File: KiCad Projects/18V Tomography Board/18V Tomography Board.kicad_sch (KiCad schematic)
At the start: 39 parts, among them J1 CONREVSMA001-G, J10 CONREVSMA001-G, J11 CONREVSMA001-G, J12 CONREVSMA001-G, J13 CONREVSMA001-G, J14 CONREVSMA001-G, J15 CONREVSMA001-G, J16 CONREVSMA001-G, J2 CONREVSMA001-G, J3 CONREVSMA001-G, J4 CONREVSMA001-G, J5 CONREVSMA001-G, J6 CONREVSMA001-G, J7 CONREVSMA001-G, J8 CONREVSMA001-G, J9 CONREVSMA001-G, U1 HV2707T-C/R8X, U2 HV2707T-C/R8X, U3 OPA365xxDBV, U4 OPA365xxDBV

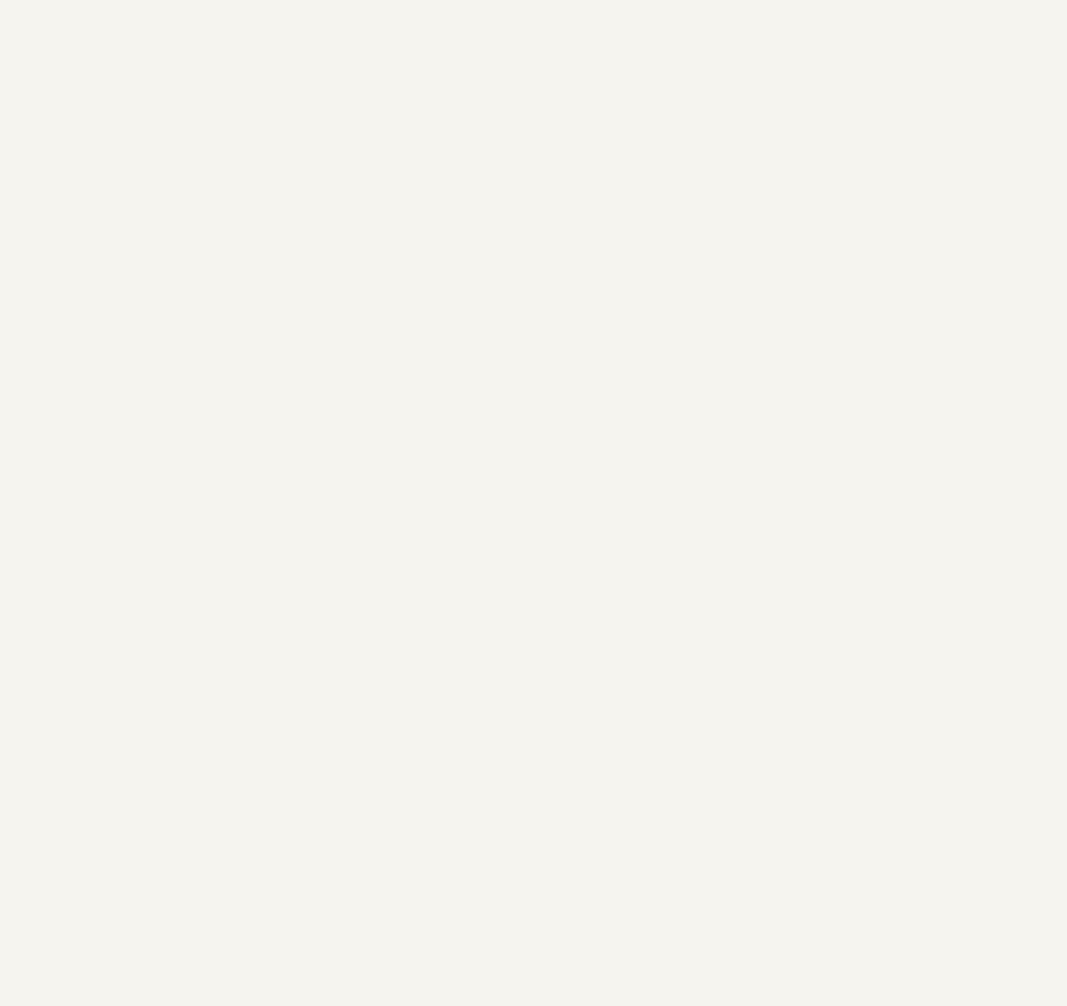
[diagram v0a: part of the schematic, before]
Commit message: added a new project and a new components for the updated pico breakout board
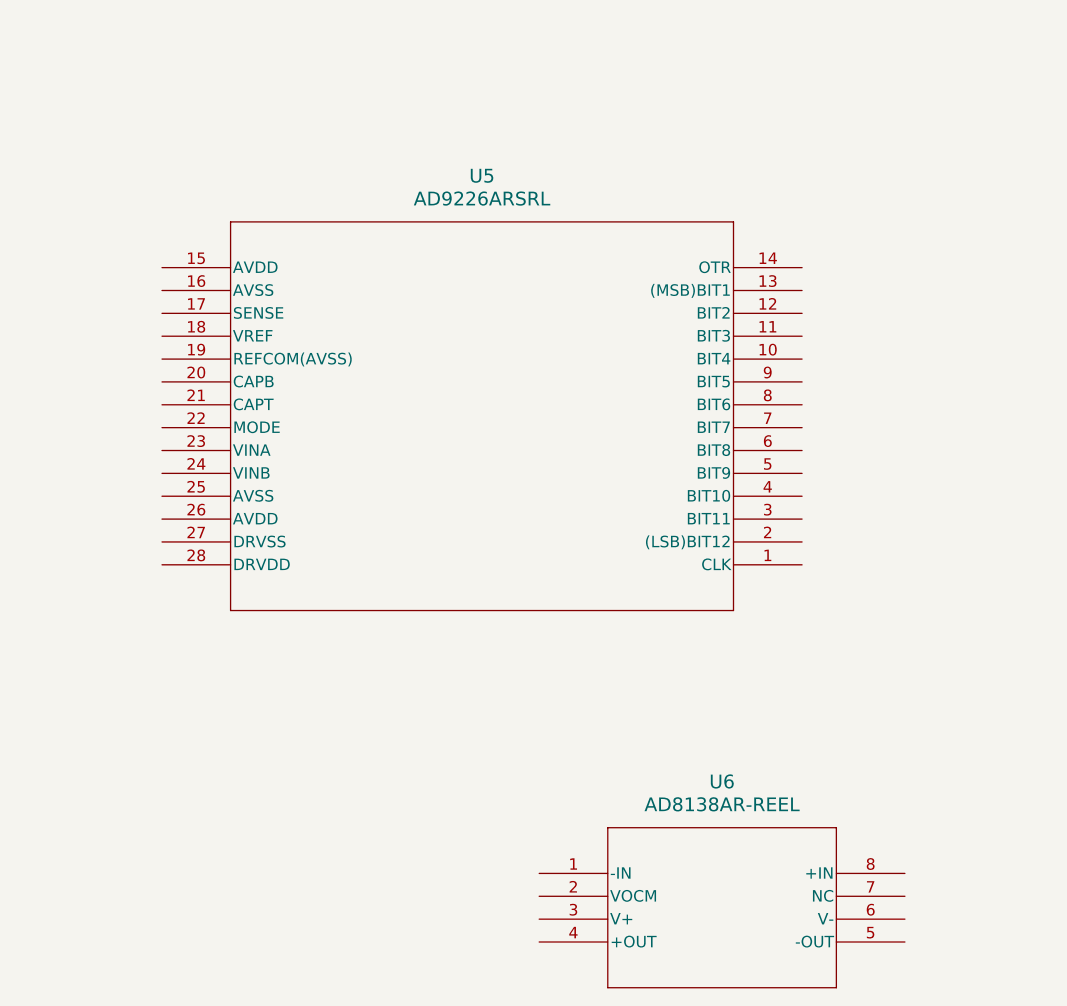
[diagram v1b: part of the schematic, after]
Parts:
- added U5: AD9226ARSRL, RS_28_ADI, symbol AD9226:AD9226ARSRL
- added U6: AD8138AR-REEL, R_8_ADI, symbol AD8138:AD8138AR-REEL
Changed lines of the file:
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@@
+	)
+	(symbol
+		(lib_id "AD8138:AD8138AR-REEL")
+		(at 537.21 679.45 0)
+		(unit 1)
+		(body_style 1)
+		(exclude_from_sim no)
+		(in_bom yes)
+		(on_board yes)
+		(in_pos_files yes)
+		(dnp no)
+		(fields_autoplaced yes)
+		(property "Reference" "U6"
+			(at 557.53 669.29 0)
+			(show_name no)
+			(do_not_autoplace no)
+			(effects
+				(font
+					(size 1.524 1.524)
+				)
+			)
+		)
+		(property "Value" "AD8138AR-REEL"
+			(at 557.53 671.83 0)
+			(show_name no)
+			(do_not_autoplace no)
+			(effects
+				(font
+					(size 1.524 1.524)
+				)
+			)
+		)
+		(property "Footprint" "R_8_ADI"
+			(at 537.21 679.45 0)
+			(hide yes)
+			(show_name no)
+			(do_not_autoplace no)
+			(effects
+				(font
+					(size 1.27 1.27)
+					(italic yes)
+				)
+			)
+		)
+		(property "Datasheet" "AD8138AR-REEL"
+			(at 537.21 679.45 0)
+			(hide yes)
+			(show_name no)
+			(do_not_autoplace no)
+			(effects
+				(font
+					(size 1.27 1.27)
+					(italic yes)
+				)
+			)
+		)
+		(property "Description" ""
+			(at 537.21 679.45 0)
+			(hide yes)
+			(show_name no)
+			(do_not_autoplace no)
+			(effects
+				(font
+					(size 1.27 1.27)
+				)
+			)
+		)
+		(pin "6"
+		)
+		(pin "2"
+		)
+		(pin "5"
+		)
+		(pin "7"
+		)
+		(pin "3"
+		)
+		(pin "1"
+		)
+		(pin "8"
+		)
+		(pin "4"
+		)
+		(instances
+			(project "18V Tomography Board"
+				(path "/8ecf61f3-91a2-40b2-9601-c3a56e620970"
+					(reference "U6")
+					(unit 1)
+				)
+			)
+		)
 	)
 	(symbol
@@
 					(unit 1)
 				)
+			)
+		)
+	)
+	(symbol
+		(lib_id "AD9226:AD9226ARSRL")
+		(at 566.42 645.16 180)
+		(unit 1)
+		(body_style 1)
+		(exclude_from_sim no)
+		(in_bom yes)
+		(on_board yes)
+		(in_pos_files yes)
+		(dnp no)
+		(fields_autoplaced yes)
+		(property "Reference" "U5"
+			(at 530.86 601.98 0)
+			(show_name no)
+			(do_not_autoplace no)
+			(effects
+				(font
+					(size 1.524 1.524)
+				)
+			)
+		)
+		(property "Value" "AD9226ARSRL"
+			(at 530.86 604.52 0)
+			(show_name no)
+			(do_not_autoplace no)
+			(effects
+				(font
+					(size 1.524 1.524)
+				)
+			)
+		)
+		(property "Footprint" "RS_28_ADI"
+			(at 566.42 645.16 0)
+			(hide yes)
+			(show_name no)
+			(do_not_autoplace no)
+			(effects
+				(font
+					(size 1.27 1.27)
+					(italic yes)
+				)
+			)
+		)
+		(property "Datasheet" "AD9226ARSRL"
+			(at 566.42 645.16 0)
+			(hide yes)
+			(show_name no)
+			(do_not_autoplace no)
+			(effects
+				(font
+					(size 1.27 1.27)
+					(italic yes)
+				)
+			)
+		)
+		(property "Description" ""
+			(at 566.42 645.16 0)
+			(hide yes)
+			(show_name no)
+			(do_not_autoplace no)
+			(effects
+				(font
+					(size 1.27 1.27)
+				)
+			)
+		)
+		(pin "3"
+		)
+		(pin "17"
+		)
+		(pin "13"
+		)
+		(pin "24"
+		)
+		(pin "19"
+		)
+		(pin "8"
+		)
+		(pin "7"
+		)
+		(pin "20"
+		)
+		(pin "21"
+		)
+		(pin "22"
+		)
+		(pin "14"
+		)
+		(pin "26"
+		)
+		(pin "5"
+		)
+		(pin "12"
+		)
+		(pin "25"
+		)
+		(pin "16"
+		)
+		(pin "28"
+		)
+		(pin "11"
+		)
+		(pin "23"
+		)
+		(pin "9"
+		)
+		(pin "1"
+		)
+		(pin "27"
+		)
+		(pin "2"
+		)
+		(pin "6"
+		)
+		(pin "10"
+		)
+		(pin "4"
+		)
+		(pin "15"
+		)
+		(pin "18"
+		)
+		(instances
+			(project "18V Tomography Board"
+				(path "/8ecf61f3-91a2-40b2-9601-c3a56e620970"
+					(reference "U5")
+					(unit 1)
+				)
